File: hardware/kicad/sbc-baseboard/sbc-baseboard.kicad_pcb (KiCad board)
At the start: 4 copper layers, 140 x 100 mm, 339 parts, among them J1 USB-C upstream, J10 RJ45 magjack 10/100, J11 COM/NO/NC, J12 COM/NO/NC, J13 Console, J14 +5V_TGT out, J15 GPIO + I2C, J16 SWD, J17 Qwiic PD, J18 PSU in (isolated), J19 PSU out (isolated), J2 USB-C PD in, J3 USB-C HID to target, J4 USB-A x2, J5 USB-A x2, J601 SWD (K20), J9 FTDI header, K801 G6K-2F-Y DC5, K802 G6K-2F-Y DC5, K803 JW1FSN-DC5V, Q101 2N7002, Q102 2N7002, Q801 2N7002, Q802 2N7002, Q803 AO3400A, SW201 RESET, SW601 DAP RESET, U101 STUSB4500QTR, U102 PCA9517A, U103 TPS54560BDDA, U104 TPS54560BDDA, U105 TPS62823DLC, U201 MK64FN1M0VLL12, U202 USBLC6-2SC6, U301 KSZ8081RNA, U401 USBLC6-2SC6, U402 USB2517, U403 TPS2553DBV, U404 TPS2553DBV, U405 TPS2553DBV, U406 TPS2553DBV, U407 TPS2553DBV, U408 USBLC6-2SC6, U409 USBLC6-2SC6, U410 USBLC6-2SC6, U411 USBLC6-2SC6, U501 FT231XS, U601 MK20DX128VFM5, U701 TXB0104PW, U702 TXB0108PW, U703 TXS0102DCU, U704 TPS26630RGE, U801 LTV-817, Y201 32.768kHz, Y301 25MHz, Y401 24MHz, Y601 8MHz

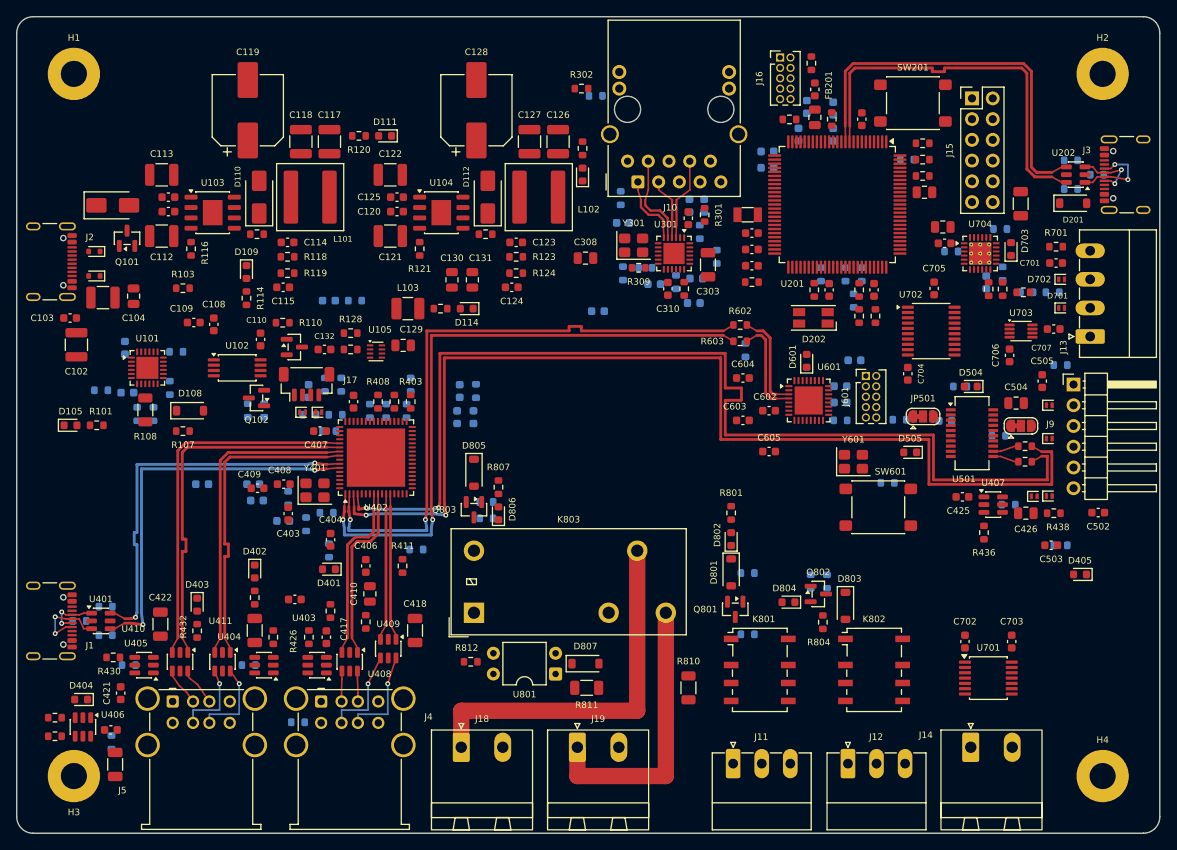
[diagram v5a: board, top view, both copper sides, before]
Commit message: The hub 5 mm down and left toward the ports; the PD controller behind J2, placed from ST's evaluation board
gen/layout.py: U402 to (39, 59) with the HUB_UP, DN1, DN2, DN4 legs following
and DN5 given a leg (U409 is no longer in line with its pins); U101 to
(16, 41) behind J2 with its CC pins toward it and the STUSB4500 template
from UM2398 Figure 24 (STEVAL-ISC005V1 top composite: decoupling above,
VBUS sense and enable right, I2C pull-ups below, reset left, top side),
U102 and J17 beside it, the 3V3 buck 3 mm left. Measured: CC pins 12-13.6 mm
from J2's CC pads, every PD part 1.6-2.5 mm from its pin, none on the
bottom; voids clean, nothing parked, DRC unchanged. Directives, the
guideline row, README and the block diagram follow; submodule to the
standard's TEMPLATED clause.

Co-Authored-By: Claude Fable 5.1 <noreply@anthropic.com>
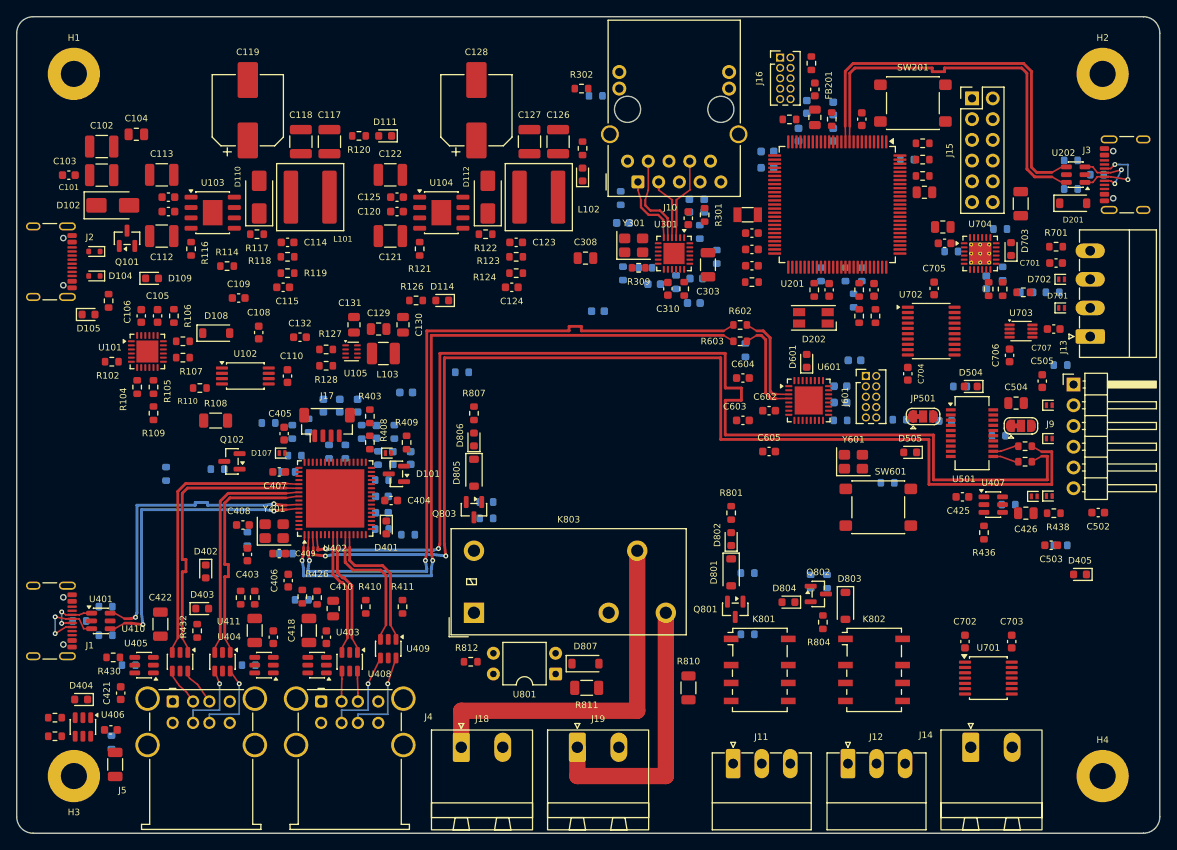
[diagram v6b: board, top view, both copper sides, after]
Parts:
- C105, C106, R102, R104, R105, R106, R109: moved to F.Cu
- moved C102 24.5 mm to (10.4, 15.9), turned to 0 degrees
- moved C415 23.6 mm to (46.1, 54.0), turned to 90 degrees
- moved D101 19.9 mm to (46.5, 56.0), turned to 180 degrees
- moved C104 19.8 mm to (14.7, 14.4), turned to 0 degrees
- moved C103 17.5 mm to (6.38, 19.4)
- moved C416 16.9 mm to (44.1, 50.8), turned to 90 degrees
- moved C412 16.2 mm to (44.7, 60.8), turned to 0 degrees
- moved R113 15.8 mm to (54.5, 43.5)
- moved C414 15.7 mm to (39.6, 47.6), turned to 90 degrees
- moved C131 15.5 mm to (41.3, 37.7)
- moved R101 15.3 mm to (11.2, 34.8), turned to 90 degrees
- moved R425 15.0 mm to (34.9, 71.4)
- moved C101 15.0 mm to (10.4, 19.4)
- moved C107 14.7 mm to (47.7, 46.0), turned to 0 degrees
- moved R111 14.3 mm to (18.3, 56.0)
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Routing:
- net HUB_DN1_P: track 77.1 -> 87.1 mm
- net /USB hub/HUB_DN7_N: track 37.8 -> 27.8 mm
- net /USB hub/HUB_DN6_N: track 44.2 -> 34.2 mm
- net /USB hub/HUB_DN7_P: track 37.9 -> 27.9 mm
- net /USB hub/HUB_UP_P: track 46.7 -> 36.7 mm
- net /USB hub/HUB_DN6_P: track 44.2 -> 34.2 mm
- net /USB hub/HUB_UP_N: track 46.7 -> 36.7 mm
- net HUB_DN2_N: track 129.2 -> 139.2 mm
- net HUB_DN1_N: track 77.1 -> 87.1 mm
- net HUB_DN2_P: track 129.2 -> 139.2 mm
- net /USB hub/HUB_DN4_N: track 21.0 -> 14.5 mm
- net /USB hub/HUB_DN4_P: track 21.0 -> 14.5 mm
- net /USB hub/HUB_DN5_P: track 17.1 -> 16.2 mm
- net /USB hub/HUB_DN5_N: track 17.1 -> 16.2 mm

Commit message: The back-row port switches and their capacitors go to the bottom, under the front-row ones
gen/layout.py: SIDES sends U404 and U406 (the stacks' back-row load switches)
to the bottom with their capacitors and pull-ups, seated above J4 and J5 on
the bottom where U403 and U405 sit on top; the port LEDs and their series
resistors stay on top. Voids clean, nothing parked, DRC unchanged; submodule
to the standard's split-channel rule.

Co-Authored-By: Claude Fable 5.1 <noreply@anthropic.com>
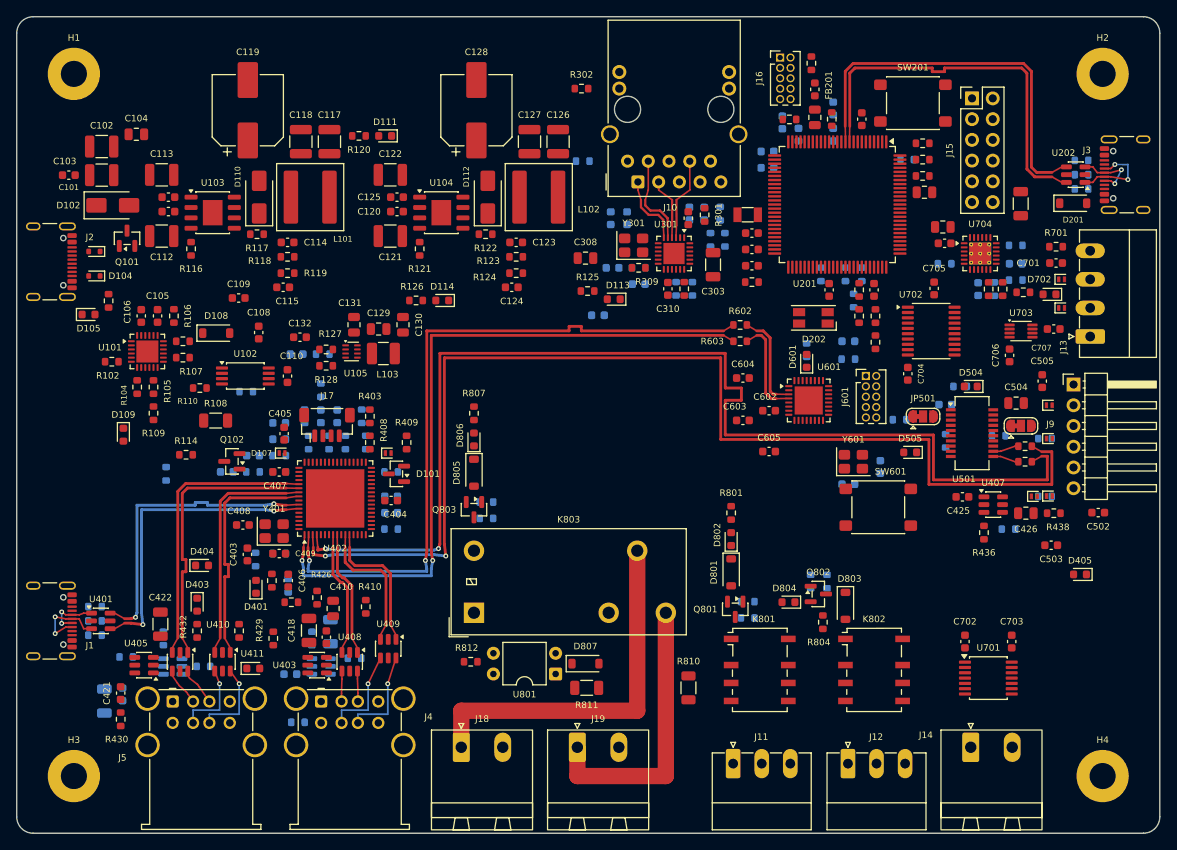
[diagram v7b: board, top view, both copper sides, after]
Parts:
- C419, C420, C423, C424, R427, R433, U404, U406: moved to B.Cu
- moved R435 26.0 mm to (27.2, 75.2), turned to 90 degrees
- moved R114 23.6 mm to (20.7, 53.6), turned to 0 degrees
- moved D404 22.1 mm to (22.7, 67.2), turned to 0 degrees
- moved D109 19.5 mm to (13.1, 51.2), turned to -90 degrees
- moved C416 19.0 mm to (25.7, 55.8), turned to 180 degrees
- moved D401 17.5 mm to (29.3, 69.8), turned to 90 degrees
- moved R125 17.5 mm to (69.9, 33.6), turned to 0 degrees
- moved R113 17.2 mm to (37.5, 41.3)
- moved C415 17.1 mm to (28.9, 53.8), turned to 180 degrees
- moved R433 16.4 mm to (18.0, 76.1), turned to -90 degrees
- moved R411 16.3 mm to (31.2, 69.1)
- moved R418 16.0 mm to (33.2, 69.7), turned to -90 degrees
- moved D113 15.7 mm to (73.1, 34.6), turned to 180 degrees
- moved R425 15.0 mm to (34.4, 86.4)
- moved R434 14.6 mm to (22.9, 79.6), turned to 0 degrees
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
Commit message: Crystals along their ICs' edges with the load capacitors flanking them; decoupling across its power traces
Regenerated under the standard's new orientation rules: the four crystals lie
along their ICs' edges with a load capacitor at each end, signal pads 1.7 to
2.1 mm from the crystal pads and toward the pins; the K64's decoupling lies
along its edges, the hub's where the rings had room. Voids clean, nothing
parked, DRC unchanged. Submodule bumped.

Co-Authored-By: Claude Fable 5.1 <noreply@anthropic.com>
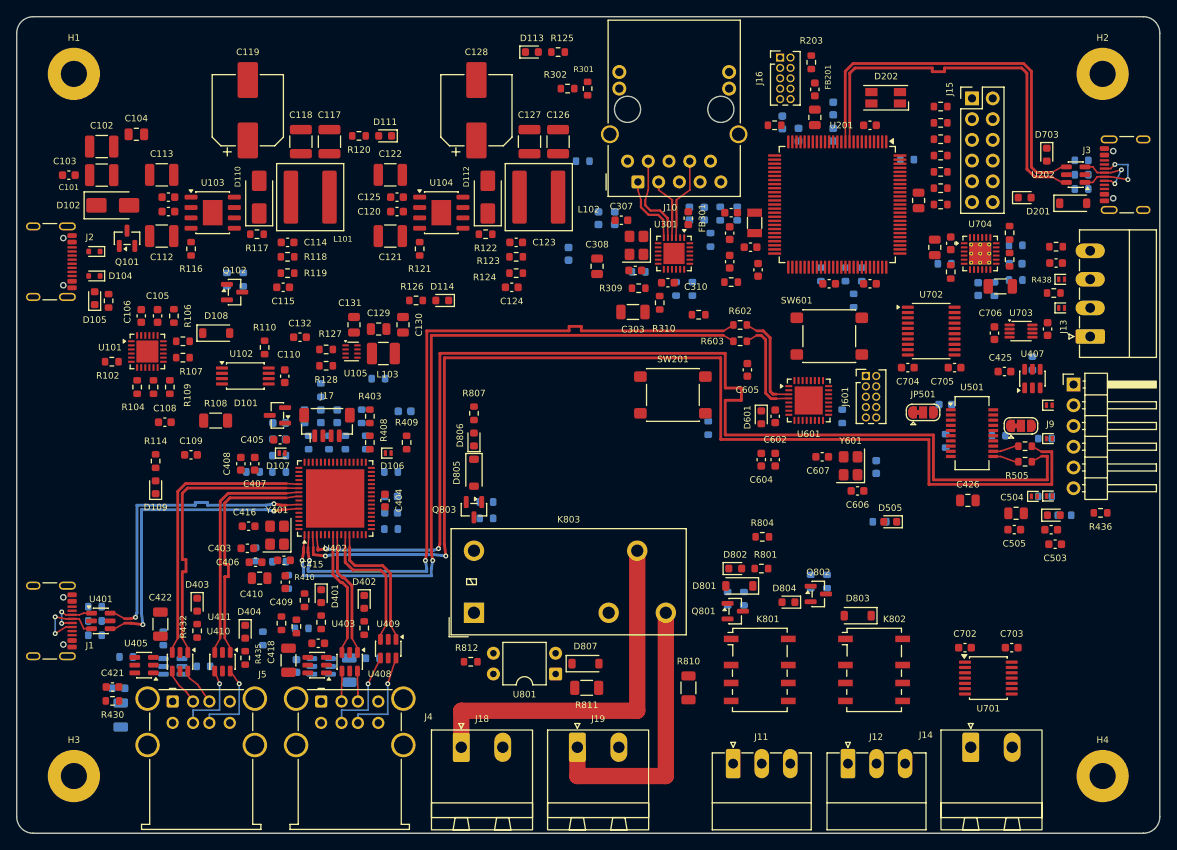
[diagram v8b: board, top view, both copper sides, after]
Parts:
- C204, C205, C306, C307, C415, C416, C606, C607: moved to F.Cu
- moved D405 46.6 mm to (123.4, 22.2), turned to 0 degrees
- moved SW201 46.3 mm to (80.4, 46.3)
- moved R217 33.8 mm to (83.5, 36.5), turned to 0 degrees
- moved D113 31.9 mm to (63.1, 4.32), turned to 0 degrees
- moved R214 29.9 mm to (113.2, 11.0), turned to 0 degrees
- moved R125 29.5 mm to (66.3, 4.32), turned to 180 degrees
- moved D202 28.4 mm to (106.4, 9.93)
- moved R438 27.0 mm to (127.0, 33.8), turned to 180 degrees
- moved R211 25.7 mm to (113.2, 13.0), turned to 0 degrees
- moved R111 24.9 mm to (25.7, 32.2), turned to 90 degrees
- moved R210 23.1 mm to (113.2, 15.0), turned to 0 degrees
- moved SW601 21.8 mm to (99.5, 39.1)
- moved R301 21.1 mm to (69.9, 8.80)
- moved Q102 20.7 mm to (26.7, 33.7), turned to 0 degrees
- moved R437 20.5 mm to (124.4, 42.4), turned to 90 degrees
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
